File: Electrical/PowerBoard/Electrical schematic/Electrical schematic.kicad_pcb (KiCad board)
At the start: 2 copper layers, 23 parts, among them J1 S4B-XH-SM4-TB, J2 XT60PW-M, J3 XT60PW-M, J5 XT60PW-M, U1 LMZ22005TZ/NOPB, U2 ACS715LLCTR-30A-T, U3 TLV2370IDBVR, U4 74LVC1G157GV_125, U5 USB-A-S-RA-TSMT

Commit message: power board V4
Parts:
- removed G***: LOGO, library:odogaron_l
- removed REF** (x4): MountingHole_2.5mm, MountingHole:MountingHole_2.5mm
- J1: footprint _Footprints:CONN4_S4B-XH_JST -> Connector_JST:JST_XH_B4B-XH-A_1x04_P2.50mm_Vertical
- moved J1 34.1 mm to (123.0, 92.5), turned to 90 degrees
- moved R4 14.3 mm to (128.0, 109.5), turned to 90 degrees
- moved C11 12.5 mm to (133.5, 104.5)
- moved C10 12.5 mm to (133.5, 109.0)
- moved U4 12.0 mm to (125.5, 99.0), turned to 0 degrees
- moved U2 11.5 mm to (142.5, 107.9)
- moved R1 11.3 mm to (149.0, 95.5)
- moved R2 11.3 mm to (149.0, 98.5)
- moved U3 11.0 mm to (125.5, 105.0), turned to 0 degrees
- moved R3 9.59 mm to (124.0, 109.5), turned to 90 degrees
- moved U5 8.73 mm to (134.5, 79.3)
- moved J5 7.47 mm to (149.4, 82.2)
- moved J2 6.25 mm to (138.1, 116.3)
- moved J3 5.00 mm to (156.6, 116.3)
- moved C1 4.02 mm to (157.0, 90.5)
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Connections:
- U1 pad 2: /Buck Converter/Vin (12V) -> GND
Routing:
- net /Buck Converter/Vout (5V 5A): track 23.0 -> 121.5 mm, vias 2 -> 0
- net /Buck Converter/Vin (12V): track 14.3 -> 51.1 mm, vias 0 -> 2
- net /Current Sensor/CURRENT IN: track 0.00 -> 18.4 mm
- net Net-(U4-S): track 30.3 -> 14.3 mm
- net Net-(U4-Y): track 34.1 -> 19.9 mm, vias 0 -> 2
- net /Current Sensor/VOLTAGE OUT (of reading): track 32.7 -> 20.1 mm, vias 4 -> 2
- net Net-(U1-FB): track 16.1 -> 7.16 mm, vias 2 -> 0
- net Net-(U3-IN-): track 9.33 -> 12.0 mm
- net Net-(U3-IN+): track 9.36 -> 7.49 mm
- net Net-(U2-FILTER): track 7.12 -> 5.46 mm
- removed copper zone on F.Cu, net /Buck Converter/Vout (5V 5A)

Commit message: Adding Vias
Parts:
- added REF**: MountingHole_2.5mm, MountingHole:MountingHole_2.5mm, F.Cu at (122.5, 68.0)
- added REF**: MountingHole_2.5mm, MountingHole:MountingHole_2.5mm, F.Cu at (122.5, 130.5)
- added REF**: MountingHole_2.5mm, MountingHole:MountingHole_2.5mm, F.Cu at (165.0, 130.5)
- added REF**: MountingHole_2.5mm, MountingHole:MountingHole_2.5mm, F.Cu at (165.0, 68.0)
- moved U5 3.50 mm to (138.0, 79.3)
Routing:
- net /Buck Converter/Vout (5V 5A): track 121.5 -> 116.9 mm

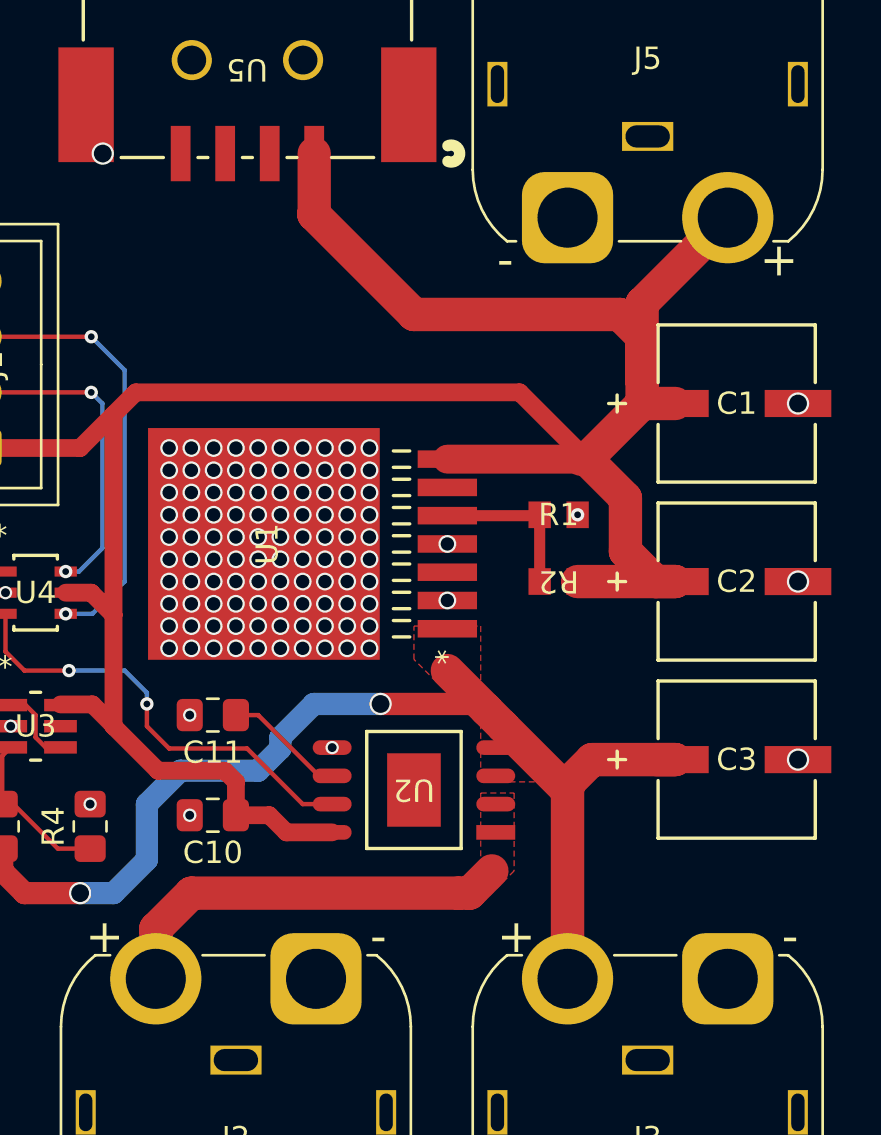
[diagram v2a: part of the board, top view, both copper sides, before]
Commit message: Bigger Traces
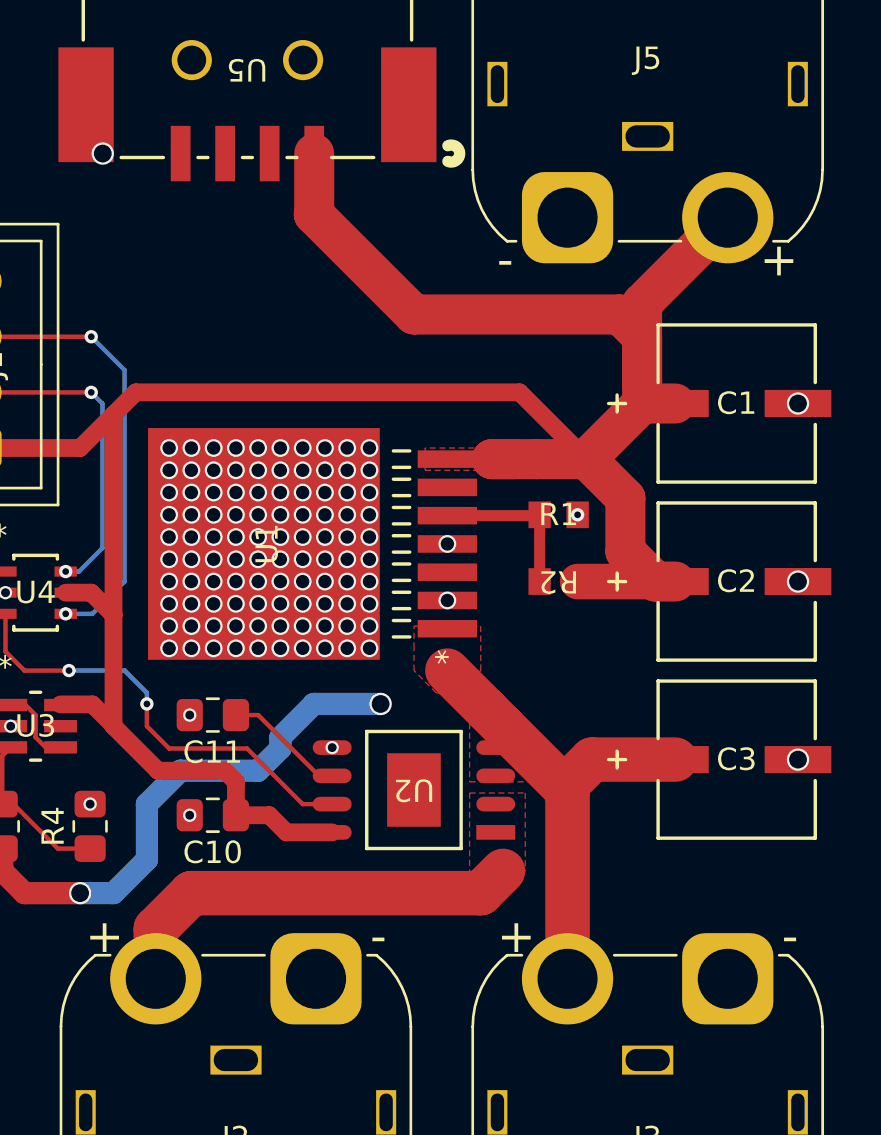
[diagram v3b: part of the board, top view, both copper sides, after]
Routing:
- net /Buck Converter/Vin (12V): track 51.1 -> 46.3 mm
- net /Buck Converter/Vout (5V 5A): track 116.9 -> 115.6 mm
- net /Current Sensor/CURRENT IN: track 18.4 -> 18.9 mm
- added copper zone on F.Cu, net /Buck Converter/Vout (5V 5A)

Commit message: connector boards
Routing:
- net /Buck Converter/Vin (12V): track 46.3 -> 51.1 mm
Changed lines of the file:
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@@
+	)
+	(segment
+		(start 141 104)
+		(end 145.5 104)
+		(width 1)
+		(layer "F.Cu")
+		(net 4)
 	)
 	(segment
@@
 		(layer "F.Cu")
 		(net 4)
+	)
+	(segment
+		(start 145.5 104)
+		(end 145.75 104.25)
+		(width 1)
+		(layer "F.Cu")
+		(net 4)

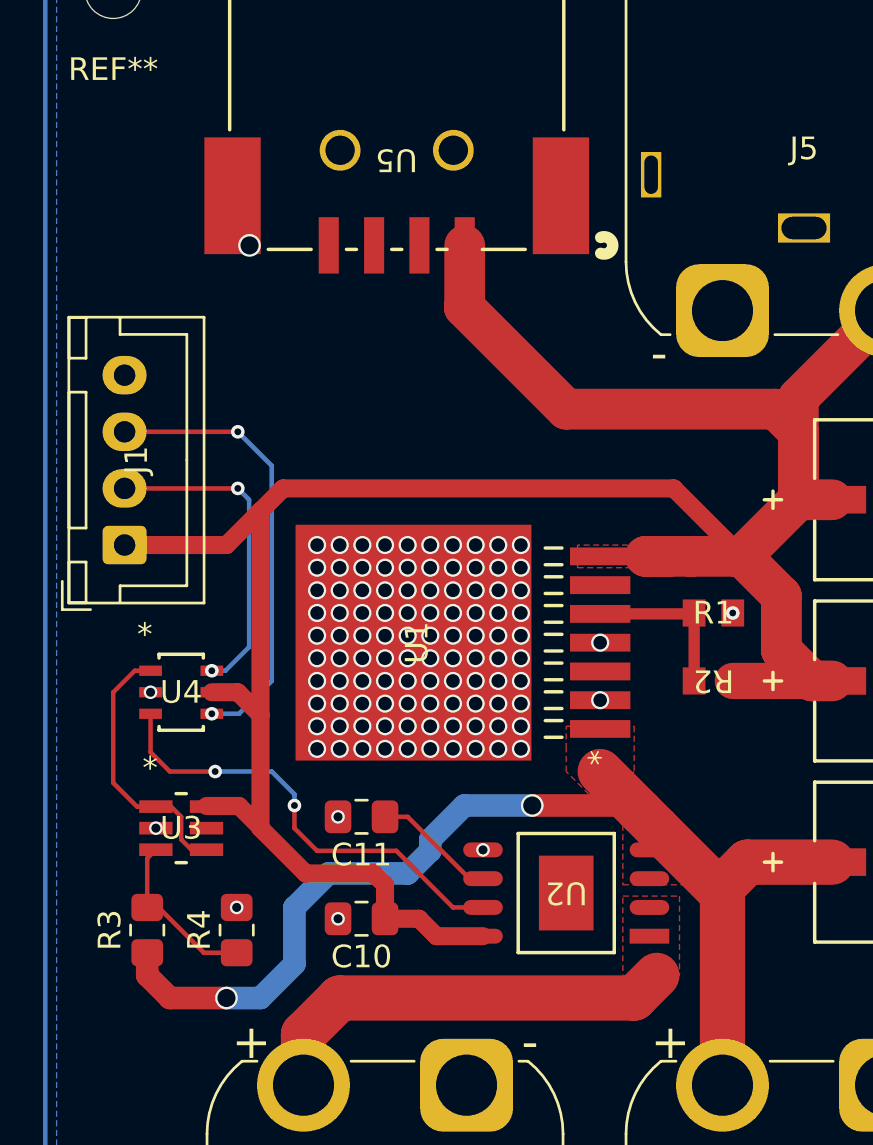
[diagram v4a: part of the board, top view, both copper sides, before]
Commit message: Buck Board Version 1
Added capacitor for Pi rail
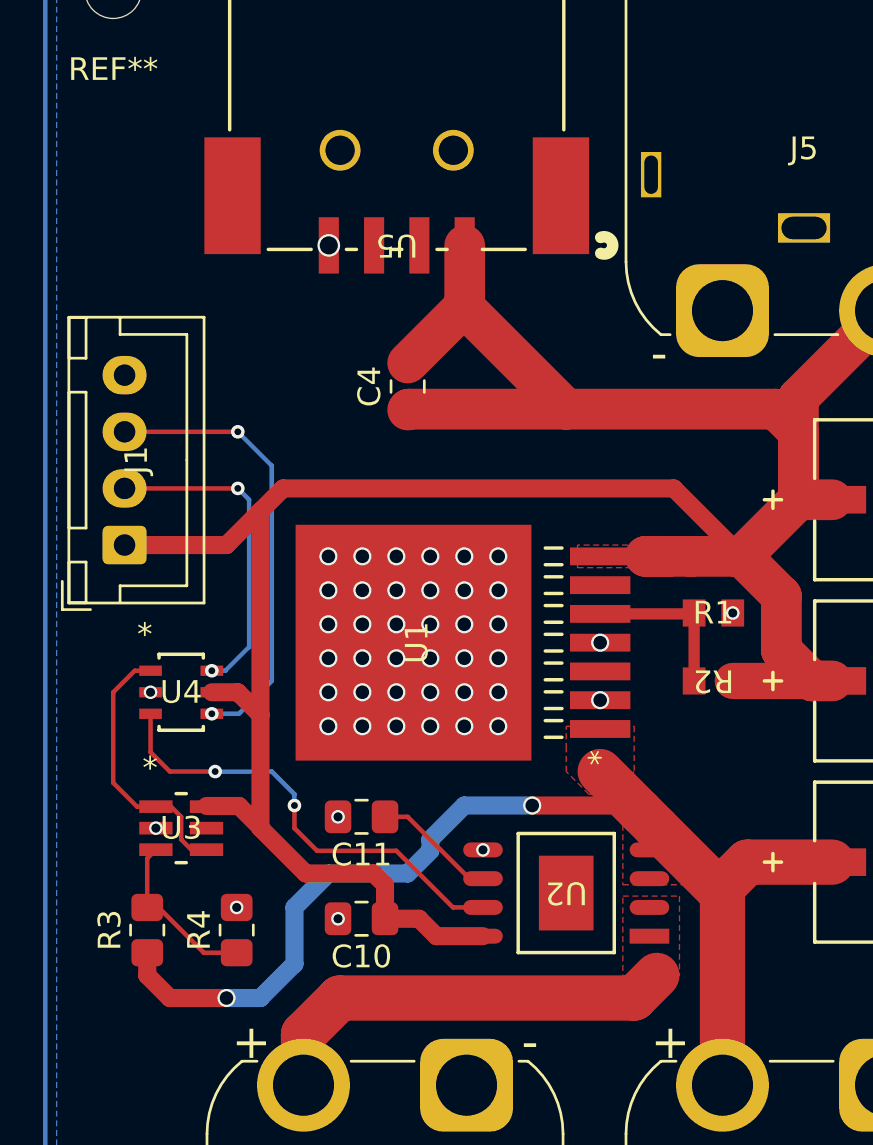
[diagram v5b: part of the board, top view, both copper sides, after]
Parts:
- added C4: 330uF, Capacitor_SMD:C_0805_2012Metric_Pad1.18x1.45mm_HandSolder, F.Cu at (135.5, 85.5)
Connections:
- U1 pad 8: unconnected-(U1-Pad8) -> GND
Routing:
- net /Buck Converter/Vout (5V 5A): track 115.6 -> 126.2 mm
- net unconnected-(U1-Pad8): vias 100 -> 0
- net GND: vias 13 -> 49

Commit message: powerboard design
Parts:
- moved C4 4.12 mm to (139.5, 86.5), turned to 0 degrees
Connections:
- C4 pad 1: /Buck Converter/Vout (5V 5A) -> GND
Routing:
- net /Buck Converter/Vout (5V 5A): track 126.2 -> 117.6 mm
- net GND: vias 49 -> 50
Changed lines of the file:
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@@
 			)
 		)
-		(fp_text user "${REFERENCE}"
-			(at 0 0 0)
+		(fp_text user "*"
+			(at -1.3716 -2.6518 0)
 			(unlocked yes)
 			(layer "F.Fab")
@@
 		(fp_text user "*"
 			(at -1.3716 -2.6518 0)
-			(unlocked yes)
 			(layer "F.Fab")
 			(effects
@@
 			)
 		)
-		(fp_text user "*"
-			(at -1.3716 -2.6518 0)
+		(fp_text user "${REFERENCE}"
+			(at 0 0 0)
+			(unlocked yes)
 			(layer "F.Fab")
 			(effects
@@
 	(footprint "Capacitor_SMD:C_0805_2012Metric_Pad1.18x1.45mm_HandSolder"
 		(layer "F.Cu")
-		(at 135.5 85.5 90)
+		(at 139.5 86.5)
 		(descr "Capacitor SMD 0805 (2012 Metric), square (rectangular) end terminal, IPC_7351 nominal with elongated pad for handsoldering. (Body size source: IPC-SM-782 page 76, https://www.pcb-3d.com/wordpress/wp-content/uploads/ipc-sm-782a_amendment_1_and_2.pdf, https://docs.google.com/spreadsheets/d/1BsfQQcO9C6DZCsRaXUlFlo91Tg2WpOkGARC1WS5S8t0/edit?usp=sharing), generated with kicad-footprint-generator")
 		(tags "capacitor handsolder")
 		(property "Reference" "C4"
-			(at 0 -1.68 90)
+			(at 0 -1.68 360)
 			(layer "F.SilkS")
 			(effects
@@
 		)
 		(property "Value" "330uF"
-			(at 0 1.68 90)
+			(at 0 1.68 360)
 			(layer "F.Fab")
 			(effects
@@
 		)
 		(property "Footprint" "Capacitor_SMD:C_0805_2012Metric_Pad1.18x1.45mm_HandSolder"
-			(at 0 0 90)
+			(at 0 0 0)
 			(unlocked yes)
 			(layer "F.Fab")
@@
 		)
 		(property "Datasheet" ""
-			(at 0 0 90)
+			(at 0 0 0)
 			(unlocked yes)
 			(layer "F.Fab")
@@
 		)
 		(property "Description" "Unpolarized capacitor"
-			(at 0 0 90)
+			(at 0 0 0)
 			(unlocked yes)
 			(layer "F.Fab")
@@
 		)
 		(fp_line
-			(start 1.88 -0.98)
-			(end 1.88 0.98)
+			(start -1.88 -0.98)
+			(end 1.88 -0.98)
 			(stroke
 				(width 0.05)
@@
 		)
 		(fp_line
-			(start -1.88 -0.98)
-			(end 1.88 -0.98)
+			(start -1.88 0.98)
+			(end -1.88 -0.98)
 			(stroke
 				(width 0.05)
@@
 		)
 		(fp_line
-			(start 1.88 0.98)
-			(end -1.88 0.98)
+			(start 1.88 -0.98)
+			(end 1.88 0.98)
 			(stroke
 				(width 0.05)
@@
 		)
 		(fp_line
-			(start -1.88 0.98)
-			(end -1.88 -0.98)
+			(start 1.88 0.98)
+			(end -1.88 0.98)
 			(stroke
 				(width 0.05)
@@
 		)
 		(fp_line
-			(start 1 -0.625)
-			(end 1 0.625)
+			(start -1 -0.625)
+			(end 1 -0.625)
 			(stroke
 				(width 0.1)
@@
 		)
 		(fp_line
-			(start -1 -0.625)
-			(end 1 -0.625)
+			(start -1 0.625)
+			(end -1 -0.625)
 			(stroke
 				(width 0.1)
@@
 		)
 		(fp_line
-			(start 1 0.625)
-			(end -1 0.625)
+			(start 1 -0.625)
+			(end 1 0.625)
 			(stroke
 				(width 0.1)
@@
 		)
 		(fp_line
-			(start -1 0.625)
-			(end -1 -0.625)
+			(start 1 0.625)
+			(end -1 0.625)
 			(stroke
 				(width 0.1)
@@
 		)
 		(fp_text user "${REFERENCE}"
-			(at 0 0 90)
+			(at 0 0 360)
 			(layer "F.Fab")
 			(effects
@@
 		)
 		(pad "1" smd roundrect
-			(at -1.0375 0 90)
+			(at -1.0375 0)
 			(size 1.175 1.45)
 			(layers "F.Cu" "F.Paste" "F.Mask")
 			(roundrect_rratio 0.212766)
-			(net 10 "/Buck Converter/Vout (5V 5A)")
+			(net 1 "GND")
 			(pintype "passive")
 		)
 		(pad "2" smd roundrect
-			(at 1.0375 0 90)
+			(at 1.0375 0)
 			(size 1.175 1.45)
 			(layers "F.Cu" "F.Paste" "F.Mask")
@@
 		(fp_text user "*"
 			(at -5.08 8.0899 90)
+			(unlocked yes)
 			(layer "F.SilkS")
 			(effects
@@
 		(fp_text user "*"
 			(at -5.08 8.0899 90)
-			(unlocked yes)
 			(layer "F.SilkS")
 			(effects
@@
 			)
 		)
-		(fp_text user "${REFERENCE}"
-			(at 0 0 90)
+		(fp_text user "*"
+			(at -5.08 8.0899 90)
 			(unlocked yes)
 			(layer "F.Fab")
@@
 			)
 		)
-		(fp_text user "*"
-			(at -5.08 8.0899 90)
+		(fp_text user "${REFERENCE}"
+			(at 0 0 90)
 			(unlocked yes)
 			(layer "F.Fab")
@@
 		(fp_text user "*"
 			(at -1.60655 -2.5502 0)
+			(unlocked yes)
 			(layer "F.SilkS")
 			(effects
@@
 		(fp_text user "*"
 			(at -1.60655 -2.5502 0)
-			(unlocked yes)
 			(layer "F.SilkS")
 			(effects
@@
 			)
 		)
-		(fp_text user "*"
-			(at -0.4699 -1.4732 0)
+		(fp_text user "${REFERENCE}"
+			(at 0 0 0)
 			(unlocked yes)
 			(layer "F.Fab")
@@
 			)
 		)
-		(fp_text user "${REFERENCE}"
-			(at 0 0 0)
+		(fp_text user "*"
+			(at -0.4699 -1.4732 0)
 			(unlocked yes)
 			(layer "F.Fab")
@@
 	)
 	(via
+		(at 138.4625 86.5)
+		(size 0.8)
+		(drill 0.6)
+		(layers "F.Cu" "B.Cu")
+		(net 1)
+	)
+	(via
 		(at 138 93)
 		(size 0.8)
@@
 	)
 	(segment
-		(start 135.5 84.4625)
-		(end 137.979899 81.982601)
-		(width 1.8)
-		(layer "F.Cu")
-		(net 10)
-	)
-	(segment
 		(start 152.75 90.5)
 		(end 154.2441 90.5)
@@
 	)
 	(segment
-		(start 135.5375 86.5)
-		(end 142.5 86.5)
-		(width 1.8)
-		(layer "F.Cu")
-		(net 10)
-	)
-	(segment
 		(start 131 107)
 		(end 129 105)
@@
 	)
 	(segment
-		(start 135.5 86.5375)
-		(end 135.5375 86.5)
-		(width 1.8)
-		(layer "F.Cu")
-		(net 10)
-	)
-	(segment
 		(start 137.979899 81.982601)
 		(end 138.017399 81.982601)
@@
 		(layer "F.Cu")
 		(net 10)
+	)
+	(segment
+		(start 142.5 86.5)
+		(end 140.5375 86.5)
+		(width 1.8)
+		(layer "F.Cu")
+		(net 10)
